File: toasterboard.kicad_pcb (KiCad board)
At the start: 2 copper layers, 100 x 70 mm, 28 parts, among them J1 DC, J2 Conn_01x04, J3 Conn_01x04, SW1 SW_Slide_DPDT, SW2 SW_Slide_DPDT, SW3 SW_Slide_DPDT, SW4 SW_Slide_DPDT

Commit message: fix: change diode footprints, finish connectimg stuff
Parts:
- added J4: Conn_01x02, Connector_PinHeader_1.00mm:PinHeader_1x02_P1.00mm_Vertical, F.Cu at (154.5, 85.5)
- D10, D11, D9: footprint Diode_THT:D_5KPW_P12.70mm_Horizontal -> Diode_THT:D_DO-35_SOD27_P7.62mm_Horizontal
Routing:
- net Net-(BT1--): track 234.8 -> 361.1 mm
- net Net-(D10-K): track 24.0 -> 137.9 mm
- net Net-(BT1-+): track 16.0 -> 53.1 mm
- net Net-(BT2-+): track 40.9 -> 35.3 mm
- net Net-(J2-Pin_4): track 17.9 -> 19.3 mm
- net Net-(D10-A): track 35.5 -> 34.9 mm
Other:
- board size 100 x 70 mm -> 100 x 71 mm

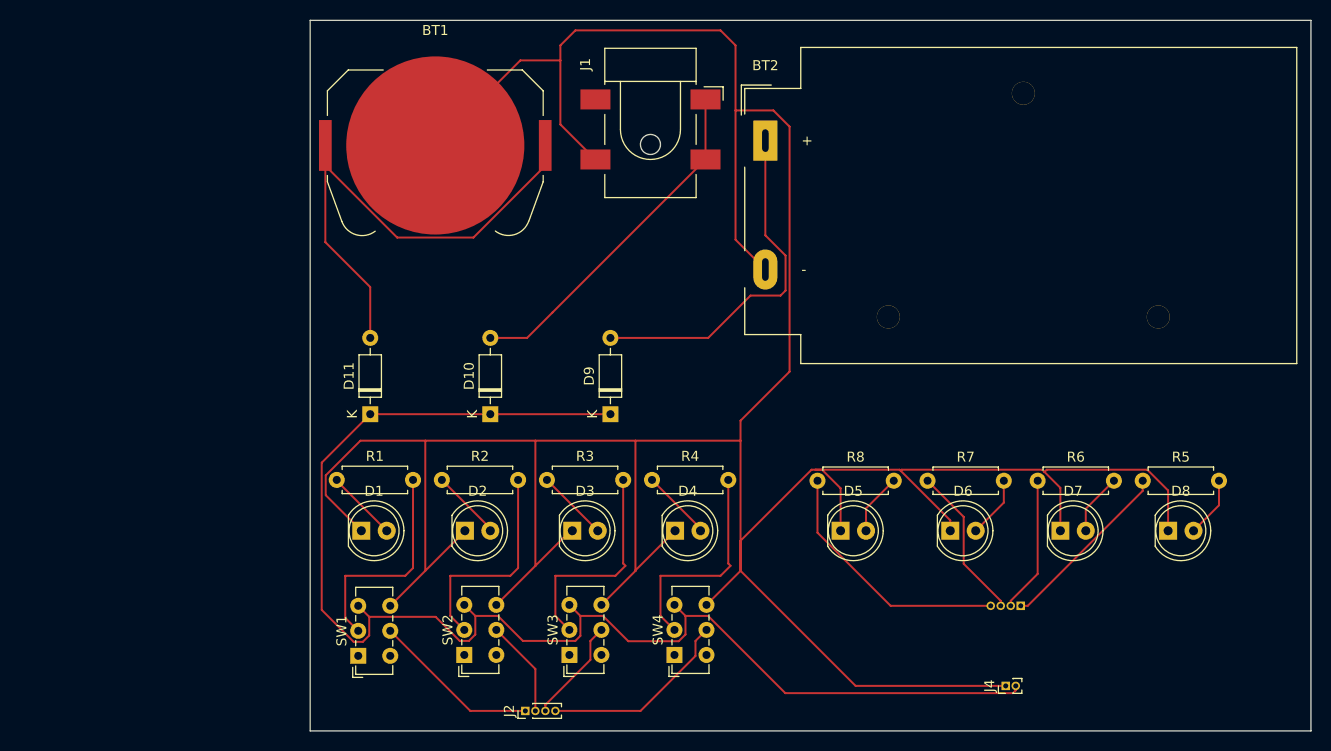
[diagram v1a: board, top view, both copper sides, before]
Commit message: feat: clean up, remove second battery
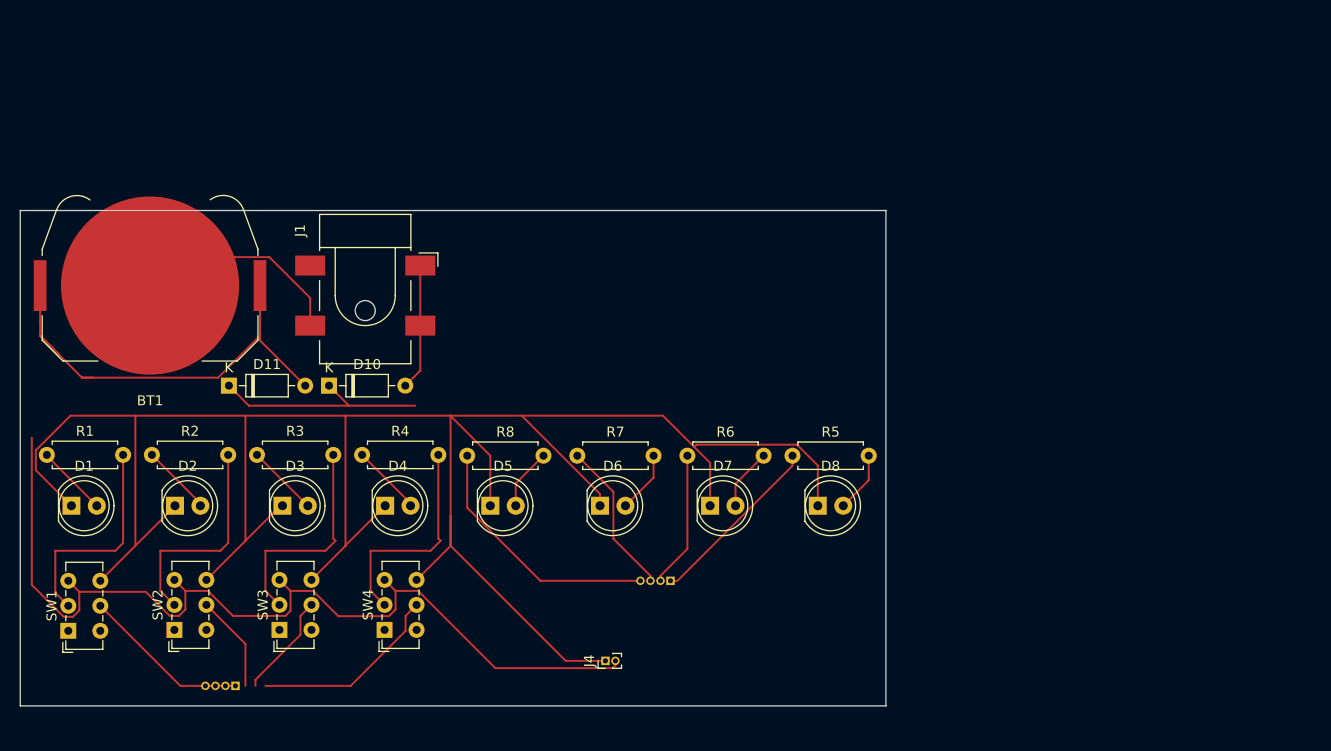
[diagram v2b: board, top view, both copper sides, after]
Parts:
- removed BT2: 9V, Battery:BatteryHolder_MPD_BA9VPC_1xPP3
- removed D9: D, Diode_THT:D_DO-35_SOD27_P7.62mm_Horizontal
- J2: moved to B.Cu
- moved J4 40.1 mm to (114.5, 83.0)
- moved D6 35.1 mm to (114.0, 67.5)
- moved D7 35.1 mm to (125.0, 67.5)
- moved D5 35.1 mm to (103.0, 67.5)
- moved D8 35.1 mm to (135.7, 67.5)
- moved J3 35.1 mm to (121.0, 75.0)
- moved R5 35.1 mm to (133.2, 62.5)
- moved R6 35.1 mm to (122.7, 62.5)
- moved R7 35.1 mm to (111.7, 62.5)
- moved R8 35.1 mm to (100.7, 62.5)
- moved J1 33.0 mm to (90.5, 46.5)
- moved BT1 31.8 mm to (69.0, 45.5), turned to 180 degrees
- moved D1 29.1 mm to (61.1, 67.5)
- moved D2 29.1 mm to (71.5, 67.5)
- moved D3 29.1 mm to (82.2, 67.5)
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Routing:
- net Net-(BT1--): track 361.1 -> 255.2 mm
- net Net-(BT2-+): track 35.3 -> 0.00 mm
- net Net-(D10-A): track 34.9 -> 12.6 mm
- net Net-(D10-K): track 137.9 -> 118.3 mm
- net Net-(BT1-+): track 53.1 -> 46.1 mm
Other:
- board size 100 x 71 mm -> 86.5 x 49.5 mm
